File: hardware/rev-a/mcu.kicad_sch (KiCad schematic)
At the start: 26 parts, among them J3 2x3 1.27, J6 MM8130-2600, U3 nRF52840, X1 32MHz, X2 32.768kHz

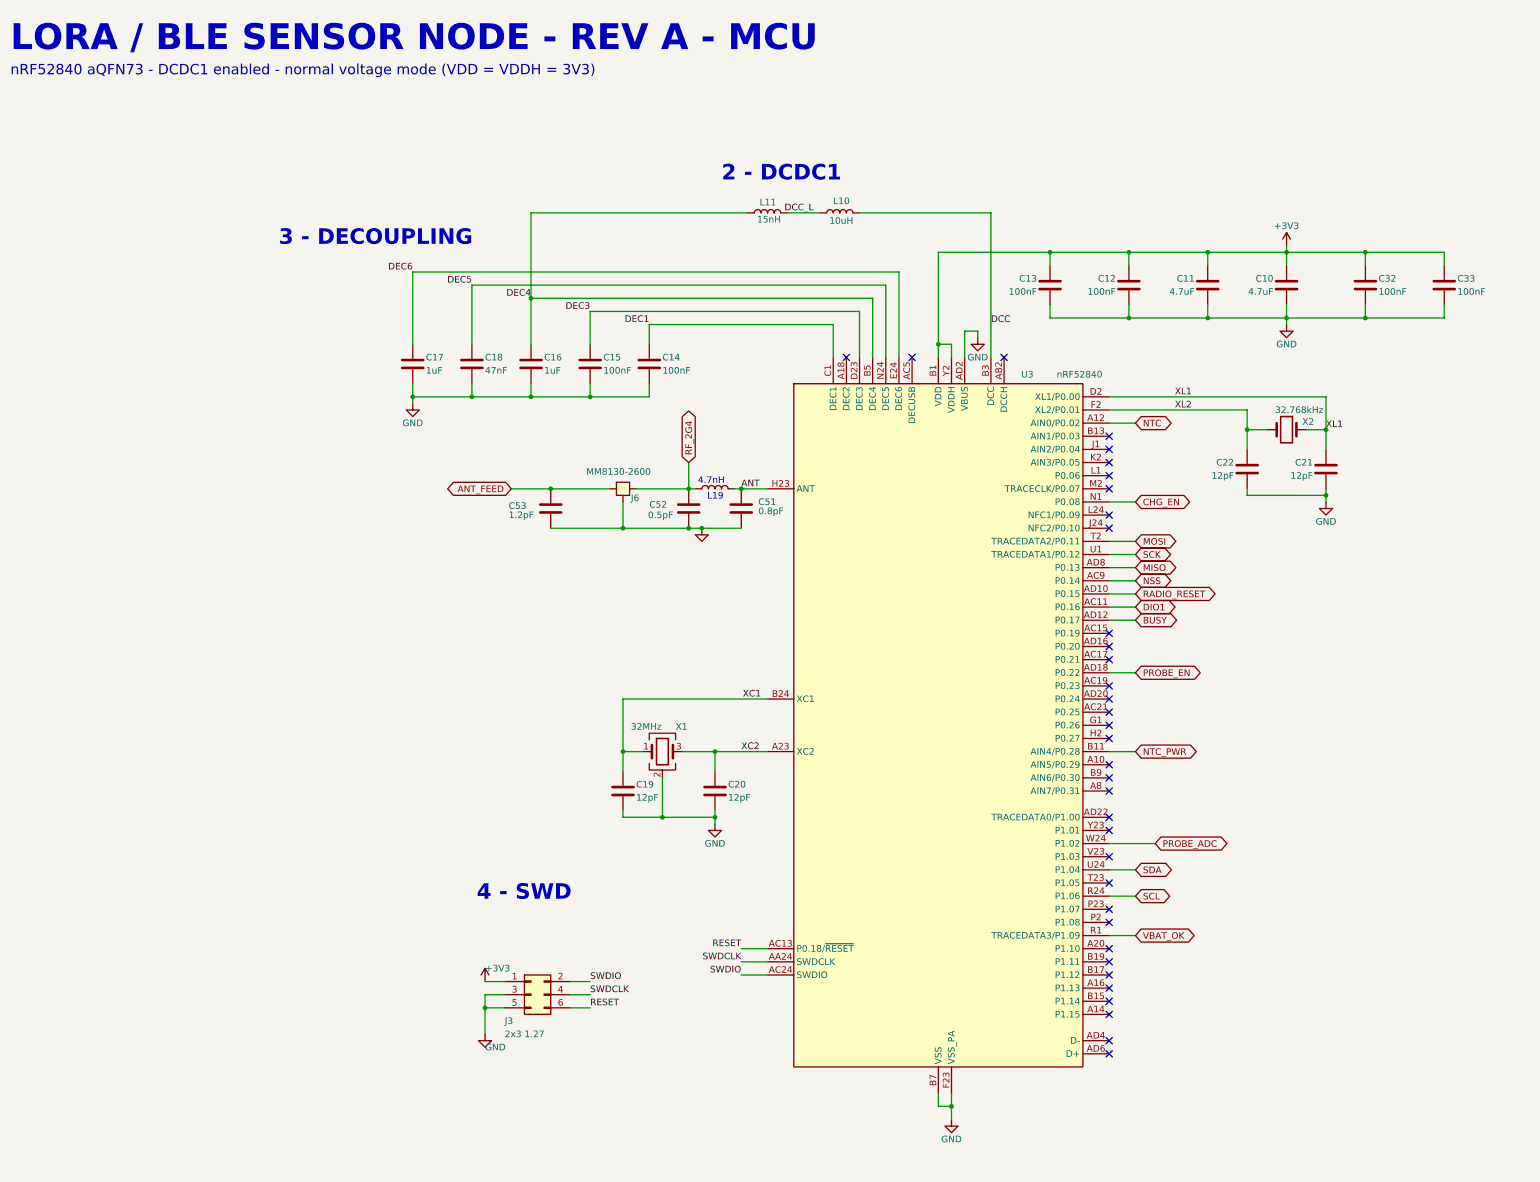
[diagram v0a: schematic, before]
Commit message: Schematic: cosmetic pass over the sheet artwork
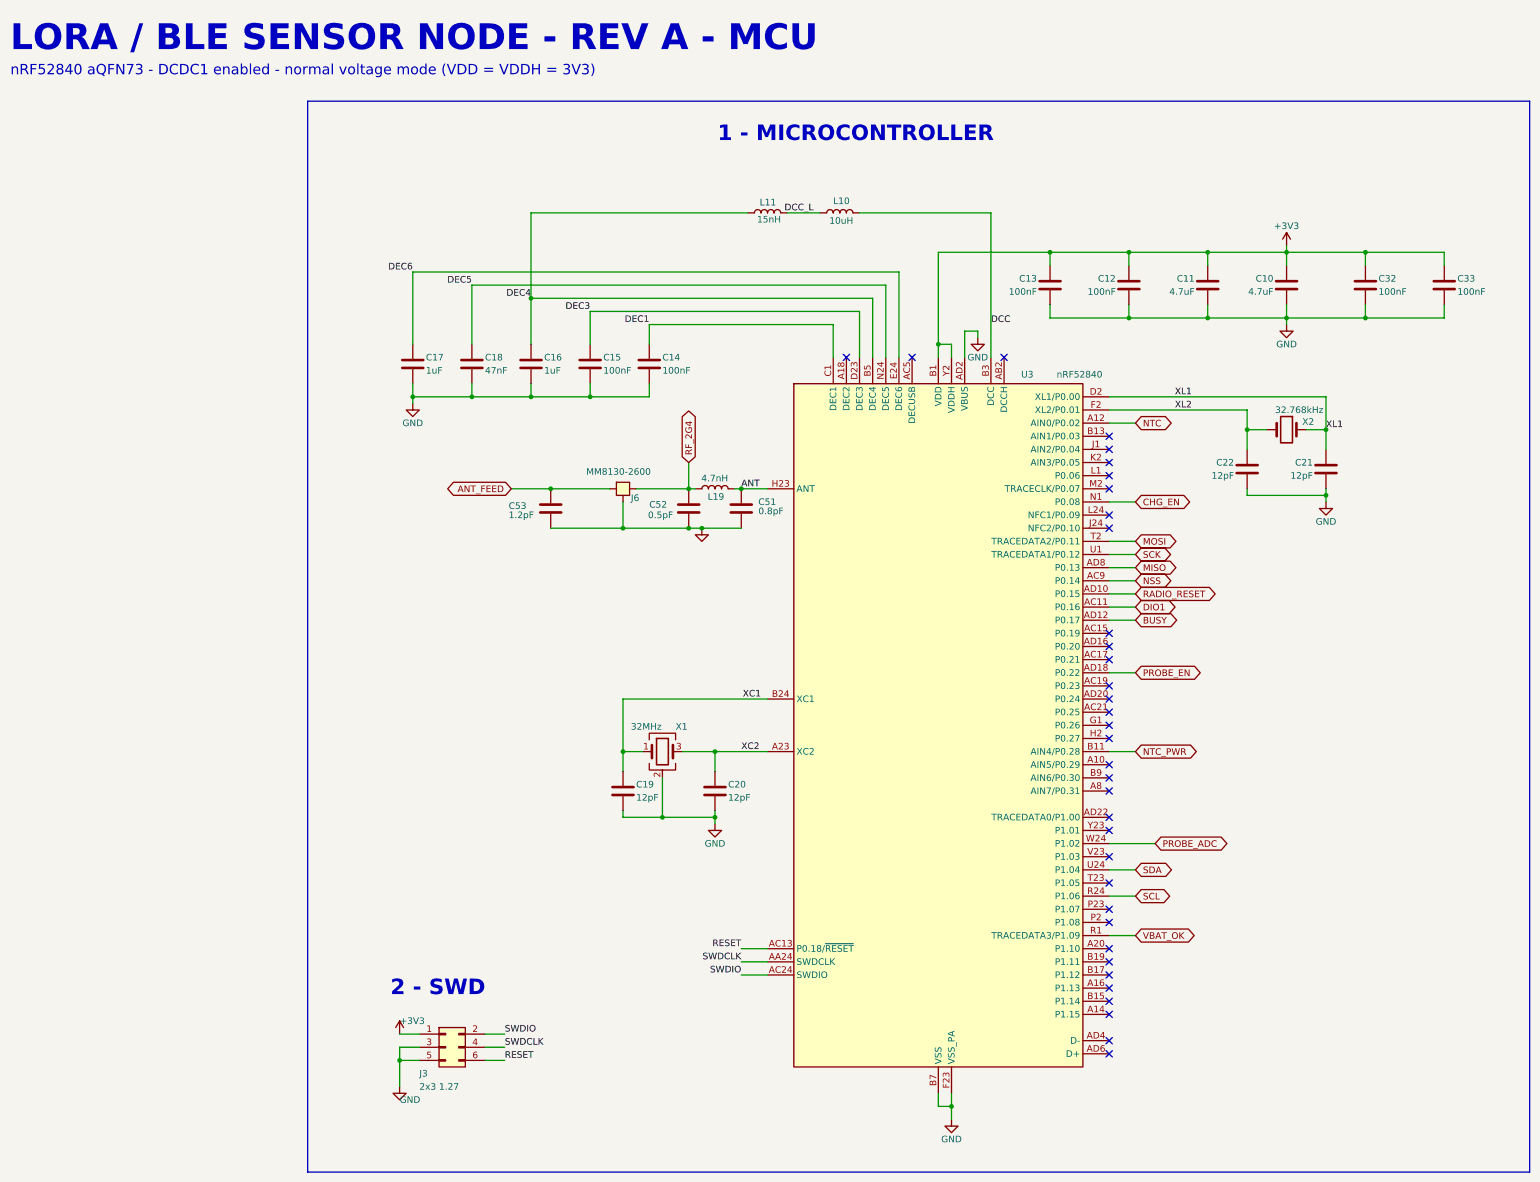
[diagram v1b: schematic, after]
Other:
- note added: "1 - MICROCONTROLLER"
- note added: "2 - SWD"
- note removed: "2 - DCDC1"
- note removed: "3 - DECOUPLING"
- note removed: "4 - SWD"
- note removed: "4.7nH"
- note removed: "L19"
- moved on the sheet: J3
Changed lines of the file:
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@@
 		(rev "A")
 		(company "Solo Engineering")
-		(comment 1 "nRF52840: 32 MHz + 32.768 kHz, DCDC1, decoupling, SWD")
+		(comment 1 "nRF52840: 32 MHz + 32.768 kHz, decoupling, SWD")
 	)
-	(text "2 - DCDC1"
-		(exclude_from_sim no)
-		(at 157.48 44.958 0)
-		(effects
-			(font
-				(size 3 3)
-				(bold yes)
-			)
-			(justify left bottom)
+	(rectangle
+		(start 77.47 29.21)
+		(end 313.69 236.22)
+		(stroke
+			(width 0)
+			(type default)
+		)
+		(fill
+			(type none)
 		)
 	)
@@
 		)
 	)
-	(text "4 - SWD"
+	(text "1 - MICROCONTROLLER"
 		(exclude_from_sim no)
-		(at 110.16 184 0)
+		(at 156.718 37.338 0)
 		(effects
 			(font
@@
 		)
 	)
-	(text "L19"
+	(text "2 - SWD"
 		(exclude_from_sim no)
-		(at 154.686 106.426 0)
-		(effects
-			(font
-				(size 1.27 1.27)
-			)
-			(justify left bottom)
-		)
-	)
-	(text "3 - DECOUPLING"
-		(exclude_from_sim no)
-		(at 71.882 57.404 0)
+		(at 93.472 202.438 0)
 		(effects
 			(font
@@
 		)
 	)
-	(text "4.7nH"
-		(exclude_from_sim no)
-		(at 152.908 103.408 0)
-		(effects
-			(font
-				(size 1.27 1.27)
-			)
-			(justify left bottom)
-		)
-	)
 	(junction
 		(at 274.32 105.41)
@@
 	)
 	(junction
-		(at 111.76 204.47)
+		(at 95.25 214.63)
 		(diameter 0)
 		(color 0 0 0 0)
@@
 	(wire
 		(pts
-			(xy 128.27 199.39) (xy 132.08 199.39)
+			(xy 111.76 209.55) (xy 115.57 209.55)
 		)
 		(stroke
@@
 	(wire
 		(pts
-			(xy 128.27 204.47) (xy 132.08 204.47)
+			(xy 111.76 214.63) (xy 115.57 214.63)
 		)
 		(stroke
@@
 	(wire
 		(pts
-			(xy 115.57 201.93) (xy 111.76 201.93)
+			(xy 99.06 212.09) (xy 95.25 212.09)
 		)
 		(stroke
@@
 	(wire
 		(pts
-			(xy 115.57 204.47) (xy 111.76 204.47)
+			(xy 99.06 214.63) (xy 95.25 214.63)
 		)
 		(stroke
@@
 	(wire
 		(pts
-			(xy 111.76 201.93) (xy 111.76 209.55)
+			(xy 95.25 212.09) (xy 95.25 219.71)
 		)
 		(stroke
@@
 	(wire
 		(pts
-			(xy 128.27 201.93) (xy 132.08 201.93)
+			(xy 111.76 212.09) (xy 115.57 212.09)
 		)
 		(stroke
@@
 	(wire
 		(pts
-			(xy 115.57 199.39) (xy 111.76 199.39)
+			(xy 99.06 209.55) (xy 95.25 209.55)
 		)
 		(stroke
@@
 	)
 	(label "SWDIO"
-		(at 132.08 199.39 0)
+		(at 115.57 209.55 0)
 		(effects
 			(font
@@
 	)
 	(label "SWDCLK"
-		(at 132.08 201.93 0)
+		(at 115.57 212.09 0)
 		(effects
 			(font
@@
 	)
 	(label "RESET"
-		(at 132.08 204.47 0)
+		(at 115.57 214.63 0)
 		(effects
 			(font
@@
 	(symbol
 		(lib_id "Connector_Generic:Conn_02x03_Odd_Even")
-		(at 120.65 201.93 0)
+		(at 104.14 212.09 0)
 		(unit 1)
 		(body_style 1)
@@
 		(dnp no)
 		(property "Reference" "J3"
-			(at 115.57 207.01 0)
+			(at 99.06 217.17 0)
 			(show_name no)
 			(do_not_autoplace no)
@@
 		)
 		(property "Value" "2x3 1.27"
-			(at 115.57 209.55 0)
+			(at 99.06 219.71 0)
 			(show_name no)
 			(do_not_autoplace no)
@@
 		)
 		(property "Footprint" "Connector_PinHeader_1.27mm:PinHeader_2x03_P1.27mm_Vertical_SMD"
-			(at 120.65 201.93 0)
+			(at 104.14 212.09 0)
 			(hide yes)
 			(show_name no)
@@
 		)
 		(property "Datasheet" "https://datasheet.lcsc.com/datasheet/pdf/1e6da833c9822e59490a6a02feaea05e.pdf?productCode=C3975186"
-			(at 120.65 201.93 0)
+			(at 104.14 212.09 0)
 			(hide yes)
 			(show_name no)
@@
 		)
 		(property "Description" "Pin Header 6 Position 1.27mm Pitch Dual Row Surface Mount -40℃~+105℃"
-			(at 120.65 201.93 0)
+			(at 104.14 212.09 0)
 			(hide yes)
 			(show_name no)
@@
 		)
 		(property "Manufacturer" "HCTL"
-			(at 0 0 0)
+			(at -16.51 10.16 0)
 			(hide yes)
 			(show_name no)
@@
 		)
 		(property "MPN" "PZ127-2-03-S"
-			(at 0 0 0)
+			(at -16.51 10.16 0)
 			(hide yes)
 			(show_name no)
@@
 		)
 		(property "LCSC" "C3975186"
-			(at 120.65 201.93 0)
+			(at 104.14 212.09 0)
 			(hide yes)
 			(show_name no)
@@
 	(symbol
 		(lib_id "power:+3V3")
-		(at 111.76 199.39 0)
+		(at 95.25 209.55 0)
 		(unit 1)
 		(body_style 1)
@@
 		(dnp no)
 		(property "Reference" "#PWR108"
-			(at 114.3 198.12 0)
+			(at 97.79 208.28 0)
 			(hide yes)
 			(show_name no)
@@
 		)
 		(property "Value" "+3V3"
-			(at 111.76 196.85 0)
+			(at 95.25 207.01 0)
 			(show_name no)
 			(do_not_autoplace no)
@@
 		)
 		(property "Footprint" ""
-			(at 111.76 199.39 0)
+			(at 95.25 209.55 0)
 			(hide yes)
 			(show_name no)
@@
 		)
 		(property "Datasheet" ""
-			(at 111.76 199.39 0)
+			(at 95.25 209.55 0)
 			(hide yes)
 			(show_name no)
@@
 		)
 		(property "Description" ""
-			(at 111.76 199.39 0)
+			(at 95.25 209.55 0)
 			(show_name no)
 			(do_not_autoplace no)
@@
 	(symbol
 		(lib_id "power:GND")
-		(at 111.76 209.55 0)
+		(at 95.25 219.71 0)
 		(unit 1)
 		(body_style 1)
@@
 		(dnp no)
 		(property "Reference" "#PWR109"
-			(at 114.3 208.28 0)
+			(at 97.79 218.44 0)
 			(hide yes)
 			(show_name no)
@@
 		)
 		(property "Value" "GND"
-			(at 111.76 212.09 0)
+			(at 95.25 222.25 0)
 			(show_name no)
 			(do_not_autoplace no)
@@
 		)
 		(property "Footprint" ""
-			(at 111.76 209.55 0)
+			(at 95.25 219.71 0)
 			(hide yes)
 			(show_name no)
@@
 		)
 		(property "Datasheet" ""
-			(at 111.76 209.55 0)
+			(at 95.25 219.71 0)
 			(hide yes)
 			(show_name no)
@@
 		)
 		(property "Description" ""
-			(at 111.76 209.55 0)
+			(at 95.25 219.71 0)
 			(show_name no)
 			(do_not_autoplace no)
@@
 		(dnp no)
 		(property "Reference" "L19"
-			(at 158.75 102.87 0)
-			(hide yes)
+			(at 157.988 105.664 90)
 			(show_name no)
 			(do_not_autoplace no)
@@
 		)
 		(property "Value" "4.7nH"
-			(at 158.75 105.41 0)
-			(hide yes)
+			(at 158.75 102.108 90)
 			(show_name no)
 			(do_not_autoplace no)
